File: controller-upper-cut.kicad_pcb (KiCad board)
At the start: 2 copper layers, 32 x 77 mm, 17 parts, among them J1 Conn_01x06_Female, J6 DB25 FEMALE, U2 74HC245, U3 74HC245, U4 ACSL-6310, U5 ACSL-6310

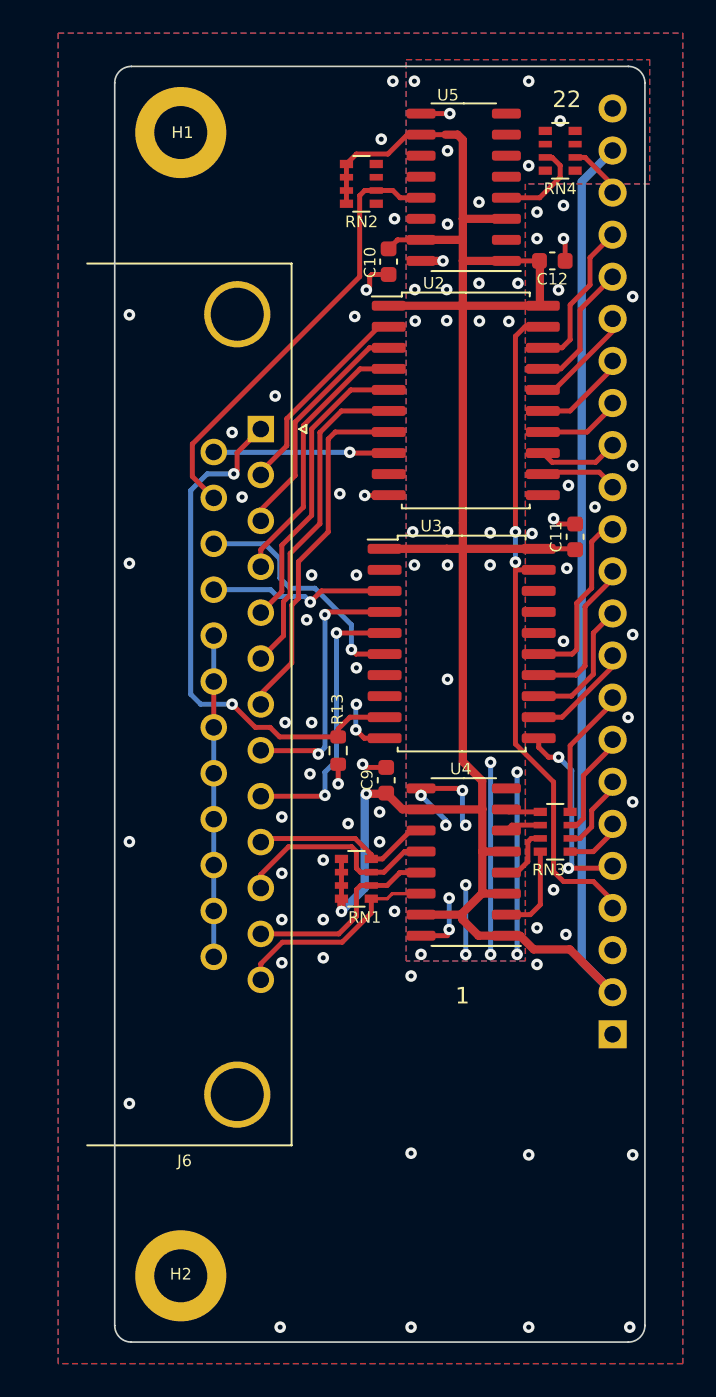
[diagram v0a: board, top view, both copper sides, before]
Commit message: v3.2 pre-production clean-up
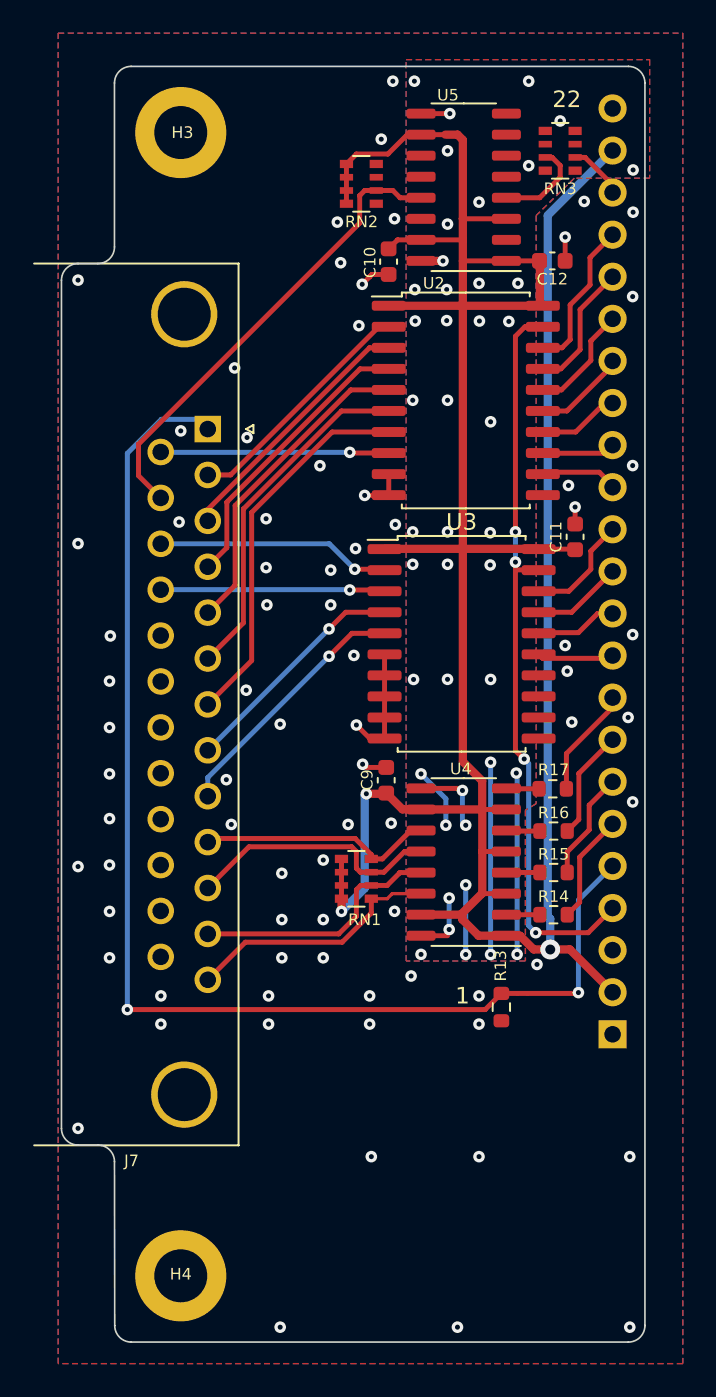
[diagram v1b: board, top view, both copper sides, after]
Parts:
- removed the RN3 at (76.6, 162.2)
- added NT1: NetTie_2, -Project:NetTie-2_SMD_Pad0.3mm, F.Cu at (74.6, 171.9)
- added R14: 330, Resistor_SMD:R_0603_1608Metric, F.Cu at (76.5, 167.2)
- added R15: 330, Resistor_SMD:R_0603_1608Metric, F.Cu at (76.5, 164.7)
- added R16: 330, Resistor_SMD:R_0603_1608Metric, F.Cu at (76.5, 162.2)
- added R17: 330, Resistor_SMD:R_0603_1608Metric, F.Cu at (76.5, 159.6)
- moved R13 18.3 mm to (73.3, 172.8)
- moved J7 3.20 mm to (55.6, 137.9)
- renumbered H1 to H3, H2 to H4, J1 to J2, J6 to J7, RN4 to RN3
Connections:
- J2 pad 3: /HOLD_IN -> unconnected-(J2-Pad3)
- U2 pad 9: unconnected-(U2-Pad9) -> GND1
- U3 pad 11: /LPT Interface/P1_OUT -> unconnected-(U3-Pad11)
- U3 pad 12: /LPT Interface/P9_OUT -> unconnected-(U3-Pad12)
- U3 pad 13: /LPT Interface/P8_OUT -> unconnected-(U3-Pad13)
- U3 pad 14: /LPT Interface/P17_OUT -> unconnected-(U3-Pad14)
- U3 pad 15: /LPT Interface/P16_OUT -> /LPT Interface/P9_OUT
- U3 pad 16: unconnected-(U3-Pad16) -> /LPT Interface/P8_OUT
- U3 pad 17: unconnected-(U3-Pad17) -> /LPT Interface/P17_OUT
- U3 pad 18: unconnected-(U3-Pad18) -> /LPT Interface/P16_OUT
- U3 pad 2: unconnected-(U3-Pad2) -> /LPT Interface/P16_IN
- U3 pad 6: /LPT Interface/P16_IN -> GND1
- U3 pad 7: unconnected-(U3-Pad7) -> GND1
- U3 pad 8: unconnected-(U3-Pad8) -> GND1
- U3 pad 9: /LPT Interface/P1_IN -> GND1
- U4 pad 7: Net-(RN3-Pad1) -> +5VA
- U4 pad 8: unconnected-(U4-Pad8) -> Net-(R17-Pad1)
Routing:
- net /LPT Interface/P1_IN: track 32.2 -> 63.5 mm, vias 2 -> 1
- net GND1: track 31.6 -> 15.3 mm, vias 64 -> 77
- net /LPT Interface/P16_OUT: track 10.9 -> 6.66 mm
- net /LPT Interface/P17_OUT: track 9.50 -> 5.49 mm
- net /LPT Interface/nCE_IN: track 41.3 -> 45.1 mm, vias 2 -> 4
- net Net-(R14-Pad1): track 5.50 -> 2.02 mm
- net /LPT Interface/P13_IN: track 3.33 -> 6.62 mm
- net /LPT Interface/P12_OUT: track 12.1 -> 15.3 mm
- net /LPT Interface/P10_OUT: track 11.1 -> 14.3 mm
- net /LPT Interface/P14_IN: track 10.6 -> 13.8 mm
- net /LPT Interface/P8_OUT: track 8.06 -> 4.96 mm
- net /LPT Interface/P11_OUT: track 12.9 -> 15.6 mm
- net /LPT Interface/P17_IN: track 10.9 -> 13.5 mm
- net /LPT Interface/P13_OUT: track 12.9 -> 15.5 mm
- net /LPT Interface/P2_IN: track 12.5 -> 14.6 mm
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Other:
- board size 32 x 77 mm -> 35.2 x 77 mm
- board text removed: "LPT INTERFACE"

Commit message: more clean-up
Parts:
- added C1: 100n/50V, Capacitor_SMD:C_0603_1608Metric, F.Cu at (74.4, 85.9)
- added C2: 1u/50V, Capacitor_SMD:C_0603_1608Metric, F.Cu at (80.1, 93.2)
- added C3: 1u/50V, Capacitor_SMD:C_0603_1608Metric, F.Cu at (51.4, 77.7)
- added C4: 100u/35V, -Project:CP_Elec_8x10.5_DOT, F.Cu at (63.6, 100.8)
- added C5: 100n/50V, Capacitor_SMD:C_0603_1608Metric, F.Cu at (66.5, 93.1)
- added C6: 100n/50V, Capacitor_SMD:C_0603_1608Metric, F.Cu at (59.5, 89.8)
- added C7: 22u/25V, Capacitor_SMD:C_1206_3216Metric, F.Cu at (71.5, 79.9)
- added C8: 68u/35V, -Project:CP_Elec_6.3x7.7_DOT, F.Cu at (71.0, 92.5)
- added D1: SDM20U40-7, Diode_SMD:D_SOD-523, F.Cu at (75.4, 90.6)
- added D2: SDM20U40-7, Diode_SMD:D_SOD-523, F.Cu at (78.2, 93.3)
- added D3: SDM20U40-7, Diode_SMD:D_SOD-523, F.Cu at (76.4, 93.3)
- added D4: SDM20U40-7, Diode_SMD:D_SOD-523, F.Cu at (77.0, 100.5)
- added D5: SDM20U40-7, Diode_SMD:D_SOD-523, F.Cu at (77.0, 102.2)
- added D6: SS24A+, -Project:D_SMA_DOT, F.Cu at (56.9, 91.6)
- added D7: BAT54JFILM, -Project:D_SOD-323_DOT, F.Cu at (70.9, 45.8)
- added H1: MountingHole_Pad, MountingHole:MountingHole_3.2mm_M3_ISO14580_Pad, F.Cu at (110.0, 120.0)
- added H2: MountingHole_Pad, MountingHole:MountingHole_3.2mm_M3_ISO14580_Pad, F.Cu at (110.0, 189.0)
- added H5: MountingHole_Pad, MountingHole:MountingHole_3.2mm_M3_ISO14580_Pad, F.Cu at (54.0, 34.0)
- added H6: MountingHole_Pad, MountingHole:MountingHole_3.2mm_M3_ISO14580_Pad, F.Cu at (54.0, 103.0)
- added H7: MountingHole_Pad, MountingHole:MountingHole_3.2mm_M3_ISO14580_Pad, F.Cu at (99.5, 34.0)
- added H8: MountingHole_Pad, MountingHole:MountingHole_3.2mm_M3_ISO14580_Pad, F.Cu at (99.5, 103.0)
- added J1: Conn_01x06_Female, Connector_PinSocket_2.54mm:PinSocket_1x23_P2.54mm_Vertical, B.Cu at (136.1, 174.4)
- added J10: Phoenix MPT, TerminalBlock_Phoenix:TerminalBlock_Phoenix_MPT-0,5-6-2.54_1x06_P2.54mm_Horizontal, F.Cu at (109.5, 75.2)
- added J11: Phoenix MPT, TerminalBlock_Phoenix:TerminalBlock_Phoenix_MPT-0,5-4-2.54_1x04_P2.54mm_Horizontal, F.Cu at (109.5, 35.8)
- added J12: MicroFit_2x04, Connector_Molex:Molex_Micro-Fit_3.0_43045-0812_2x04_P3.00mm_Vertical, F.Cu at (86.6, 51.5)
- added J13: Phoenix MPT, TerminalBlock_Phoenix:TerminalBlock_Phoenix_MPT-0,5-4-2.54_1x04_P2.54mm_Horizontal, F.Cu at (109.5, 48.8)
- added J14: MicroFit_2x04, Connector_Molex:Molex_Micro-Fit_3.0_43045-0812_2x04_P3.00mm_Vertical, F.Cu at (86.6, 70.3)
- added J15: JST_B2B-XH, TerminalBlock_Phoenix:TerminalBlock_Phoenix_MPT-0,5-4-2.54_1x04_P2.54mm_Horizontal, F.Cu at (40.7, 84.6)
- added J16: Phoenix MPT, TerminalBlock_Phoenix:TerminalBlock_Phoenix_MPT-0,5-4-2.54_1x04_P2.54mm_Horizontal, F.Cu at (109.5, 62.1)
- added J17: MicroFit_2x04, Connector_Molex:Molex_Micro-Fit_3.0_43045-0812_2x04_P3.00mm_Vertical, F.Cu at (86.6, 89.2)
- added J18: MLX_1x03, Connector_Molex:Molex_KK-254_AE-6410-03A_1x03_P2.54mm_Vertical, F.Cu at (96.7, 78.4)
- added J19: MLX_1x03, Connector_Molex:Molex_KK-254_AE-6410-03A_1x03_P2.54mm_Vertical, F.Cu at (96.7, 88.0)
- added J20: Phoenix MPT, TerminalBlock_Phoenix:TerminalBlock_Phoenix_MPT-0,5-4-2.54_1x04_P2.54mm_Horizontal, F.Cu at (40.7, 53.4)
- added J3: Conn_01x022_Male, Connector_PinHeader_2.54mm:PinHeader_1x23_P2.54mm_Vertical, F.Cu at (80.1, 88.3)
- added J4: KYCON_KPJX-4S-S, -Project:KYCON_KPJX-4S-S, F.Cu at (57.0, 65.5)
- added J5: MicroFit_2x02, Connector_Molex:Molex_Micro-Fit_3.0_43045-0412_2x02_P3.00mm_Vertical, F.Cu at (87.3, 96.9)
- added J6: 24V/5A OUT, TerminalBlock_Phoenix:TerminalBlock_Phoenix_MKDS-1,5-2-5.08_1x02_P5.08mm_Horizontal, F.Cu at (108.0, 99.7)
- added J8: Phoenix MPT, TerminalBlock_Phoenix:TerminalBlock_Phoenix_MPT-0,5-2-2.54_1x02_P2.54mm_Horizontal, F.Cu at (40.7, 77.9)
- added JP1: Jumper_2_Bridged, Connector_PinHeader_2.54mm:PinHeader_2x01_P2.54mm_Vertical, F.Cu at (97.8, 96.5)
- added JP2: GND_ISO, Connector_PinHeader_2.54mm:PinHeader_1x02_P2.54mm_Vertical, F.Cu at (90.7, 33.8)
- added JP3: 1x03_2.54, Connector_PinHeader_2.54mm:PinHeader_1x03_P2.54mm_Vertical, F.Cu at (75.4, 70.1)
- added JP4: Jumper_3_Open, Connector_PinHeader_2.54mm:PinHeader_1x03_P2.54mm_Vertical, F.Cu at (100.2, 45.6)
- added JP5: Jumper_3_Open, Connector_PinHeader_2.54mm:PinHeader_1x03_P2.54mm_Vertical, F.Cu at (100.2, 57.7)
- added JP6: 1x03_2.54, Connector_PinHeader_2.54mm:PinHeader_1x03_P2.54mm_Vertical, F.Cu at (75.4, 63.3)
- added JP7: 1x03_2.54, Connector_PinHeader_2.54mm:PinHeader_1x03_P2.54mm_Vertical, F.Cu at (75.4, 53.5)
- added JP8: Jumper_3_Open, Connector_PinHeader_2.54mm:PinHeader_1x03_P2.54mm_Vertical, F.Cu at (100.2, 68.9)
- added K1: OJS-SH-124HMF, -Project:Relay_SPST_OJS_24V_10A, F.Cu at (67.6, 45.4)
- added L1: 100uH 1.5A+, Inductor_SMD:L_12x12mm_H6mm, F.Cu at (62.5, 81.4)
- added NT22: DNI, -Project:NetTie-2_SMD_Pad0.3mm, F.Cu at (96.1, 98.5)
- added NT23: DNI, -Project:NetTie-2_SMD_Pad1.0mm, F.Cu at (59.5, 97.9)
- added NT24: DNI, -Project:NetTie-2_SMD_Pad1.0mm, F.Cu at (73.1, 82.6)
- added NT25: DNI, -Project:NetTie-2_SMD_Pad0.3mm, B.Cu at (108.3, 81.7)
- added NT26: DNI, -Project:NetTie-2_SMD_Pad0.3mm, B.Cu at (108.3, 79.1)
- added NT27: DNI, -Project:NetTie-2_SMD_Pad0.3mm, B.Cu at (111.5, 74.8)
- added NT28: DNI, -Project:NetTie-2_SMD_Pad1.0mm, B.Cu at (97.6, 64.5)
- added Q1: BC847, Package_TO_SOT_SMD:SOT-23, F.Cu at (77.7, 98.0)
- added Q2: FDD5614P, Package_TO_SOT_SMD:TO-252-2, F.Cu at (49.6, 87.1)
- added Q3: BC857, -Project:SOT-23_DOT, F.Cu at (71.6, 100.8)
- added Q4: BC847, Package_TO_SOT_SMD:SOT-23, F.Cu at (68.5, 64.0)
- added Q5: BC857, -Project:SOT-23_DOT, F.Cu at (66.0, 60.0)
- added R10: 130K, Resistor_SMD:R_0603_1608Metric, F.Cu at (74.8, 101.3)
- added R11: 1M, Resistor_SMD:R_0603_1608Metric, F.Cu at (71.5, 98.0)
- added R12: 220K, Resistor_SMD:R_0603_1608Metric, F.Cu at (66.4, 89.8)
- added R18: 5K6, Resistor_SMD:R_0603_1608Metric, F.Cu at (70.2, 60.4)
- added R19: 5K6, Resistor_SMD:R_0603_1608Metric, F.Cu at (68.5, 60.4)
- added R2: 1M, Resistor_SMD:R_0603_1608Metric, F.Cu at (77.4, 85.9)
- added R20: 10K, Resistor_SMD:R_0603_1608Metric, F.Cu at (66.0, 57.1)
- added R3: 6K8, Resistor_SMD:R_0603_1608Metric, F.Cu at (77.3, 95.4)
- added R4: 220K, Resistor_SMD:R_0603_1608Metric, F.Cu at (51.4, 79.2)
- added R5: 1K, Resistor_SMD:R_0603_1608Metric, F.Cu at (95.1, 98.2)
- added R6: 130K, Resistor_SMD:R_0603_1608Metric, F.Cu at (74.8, 98.0)
- added R7: 1M, Resistor_SMD:R_0603_1608Metric, F.Cu at (51.4, 80.7)
- added R8: 680K, Resistor_SMD:R_0603_1608Metric, F.Cu at (49.0, 79.9)
- added R9: 330K, Resistor_SMD:R_0603_1608Metric, F.Cu at (51.4, 76.2)
- added U1: MAX5035BUSA, Package_SO:SOIC-8_3.9x4.9mm_P1.27mm, F.Cu at (63.0, 92.0)
- added U6: USBLC6-2SC6, Package_TO_SOT_SMD:SOT-23-6, F.Cu at (111.0, 177.5)
- added U7: ADUM4160, Package_SO:SOIC-16W_7.5x10.3mm_P1.27mm, F.Cu at (114.8, 169.3)
- added U8: ATmega16U2-A, Package_QFP:TQFP-32_7x7mm_P0.8mm, F.Cu at (127.1, 169.2)
- added U9: ATmega328P-A, Package_QFP:TQFP-32_7x7mm_P0.8mm, F.Cu at (120.8, 150.9)
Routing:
- net +5V: track 0.00 -> 177.1 mm, vias 0 -> 1
- net 24V_SAFE: track 0.00 -> 119.1 mm, vias 0 -> 52
- net /Connectors & Jumpers/ESTOP_OUT: track 0.00 -> 78.4 mm, vias 0 -> 3
- net /Power/Q1_C: track 0.00 -> 70.0 mm, vias 0 -> 4
- net /Connectors & Jumpers/X_P16_OUT: track 0.00 -> 67.6 mm, vias 0 -> 3
- net /Connectors & Jumpers/EN_IN: track 0.00 -> 65.3 mm
- net /Connectors & Jumpers/X_P17_OUT: track 0.00 -> 53.6 mm, vias 0 -> 3
- net 24V_IN: track 0.00 -> 51.2 mm
- net /Connectors & Jumpers/ZDIR_IN: track 0.00 -> 49.7 mm, vias 0 -> 3
- net /Connectors & Jumpers/VFD_PWM: track 0.00 -> 48.9 mm, vias 0 -> 1
- net /Connectors & Jumpers/ZCLK_IN: track 0.00 -> 48.6 mm, vias 0 -> 2
- net /Connectors & Jumpers/HOLD_OUT: track 0.00 -> 45.5 mm, vias 0 -> 1
- net /Connectors & Jumpers/RELAY4: track 0.00 -> 44.4 mm, vias 0 -> 1
- net /Connectors & Jumpers/RELAY2_IN: track 0.00 -> 44.0 mm, vias 0 -> 3
- net /Connectors & Jumpers/RELAY3_IN: track 0.00 -> 42.1 mm, vias 0 -> 3
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- added copper zone on F.Cu, net /Power/U2_LX
- added copper zone on B.Cu, net 24V_SAFE
- added copper zone on F.Cu, net 24V_SAFE
- added copper zone on B.Cu, net GND
- added copper zone on F.Cu, net GND
- added copper zone on B.Cu, net GNDA
- added copper zone on F.Cu, net GNDA
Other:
- board size 35.2 x 77 mm -> 101.3 x 162.9 mm
- board text added: "* P16"
- board text added: "* P17"
- board text added: "+24V"
- board text added: "+24V IN"
- board text added: "+5V"
- board text added: "0V"
- board text added: "23"
- board text added: "24V"
- board text added: "24V/5A IN"
- board text added: "5A"
- board text added: "5V"
- board text added: "AGND"
- board text added: "BitSetter"
- board text added: "BitZero"
- board text added: "C"
- board text added: "C.P."
- board text added: "CLK"
- board text added: "COM"
- board text added: "COMMON"
- board text added: "CPO"
- board text added: "DGND"
- board text added: "DIR"
- board text added: "G"
- board text added: "JLCJLCJLCJLC"
- board text added: "LED"
- board text added: "LPT INTERFACE"
- board text added: "NC"
- board text added: "NO"
- board text added: "P1"
- board text added: "PWM 5V"
- board text added: "PWM(5V)"
- board text added: "PWR SW"
- board text added: "RELAY"
- board text added: "RELAYS"
- board text added: "RL1/E"
- board text added: "RL2"
- board text added: "RL3"
- board text added: "RL4*"
- board text added: "RLY4 *"
- board text added: "SPDL RLY"
- board text added: "SPINDLE"
- board text added: "SW"
- board text added: "Shapeoko LPT Interface v3.2"
- board text added: "USB GRBL INTERFACE"
- board text added: "X"
- board text added: "X DRV"
- board text added: "X ENDSTOP"
- board text added: "XGND"
- board text added: "Y"
- board text added: "Y DRV"
- board text added: "Y ENDSTOP"
- board text added: "YCLX"
- board text added: "Z"
- board text added: "Z DRV"
- board text added: "Z ENDSTOP"
- board text added: "ZCLX"
- board text added: "github.com/gruvin/shapeoko-lpt"
- board text removed: "22"

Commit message: commit to v3.2 production
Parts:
- removed C1, C5, C6: 100n/50V, Capacitor_SMD:C_0603_1608Metric
- removed C2, C3: 1u/50V, Capacitor_SMD:C_0603_1608Metric
- removed C4: 100u/35V, -Project:CP_Elec_8x10.5_DOT
- removed C7: 22u/25V, Capacitor_SMD:C_1206_3216Metric
- removed C8: 68u/35V, -Project:CP_Elec_6.3x7.7_DOT
- removed D1, D2, D3, D4, D5: SDM20U40-7, Diode_SMD:D_SOD-523
- removed D6: SS24A+, -Project:D_SMA_DOT
- removed D7: BAT54JFILM, -Project:D_SOD-323_DOT
- removed H1, H2, H5, H6, H7, H8: MountingHole_Pad, MountingHole:MountingHole_3.2mm_M3_ISO14580_Pad
- removed J1: Conn_01x06_Female, Connector_PinSocket_2.54mm:PinSocket_1x23_P2.54mm_Vertical
- removed J10: Phoenix MPT, TerminalBlock_Phoenix:TerminalBlock_Phoenix_MPT-0,5-6-2.54_1x06_P2.54mm_Horizontal
- removed J11, J13, J16, J20: Phoenix MPT, TerminalBlock_Phoenix:TerminalBlock_Phoenix_MPT-0,5-4-2.54_1x04_P2.54mm_Horizontal
- removed J12, J14, J17: MicroFit_2x04, Connector_Molex:Molex_Micro-Fit_3.0_43045-0812_2x04_P3.00mm_Vertical
- removed J15: JST_B2B-XH, TerminalBlock_Phoenix:TerminalBlock_Phoenix_MPT-0,5-4-2.54_1x04_P2.54mm_Horizontal
- removed J18, J19: MLX_1x03, Connector_Molex:Molex_KK-254_AE-6410-03A_1x03_P2.54mm_Vertical
- removed J3: Conn_01x022_Male, Connector_PinHeader_2.54mm:PinHeader_1x23_P2.54mm_Vertical
- removed J4: KYCON_KPJX-4S-S, -Project:KYCON_KPJX-4S-S
- removed J5: MicroFit_2x02, Connector_Molex:Molex_Micro-Fit_3.0_43045-0412_2x02_P3.00mm_Vertical
- removed J6: 24V/5A OUT, TerminalBlock_Phoenix:TerminalBlock_Phoenix_MKDS-1,5-2-5.08_1x02_P5.08mm_Horizontal
- removed J8: Phoenix MPT, TerminalBlock_Phoenix:TerminalBlock_Phoenix_MPT-0,5-2-2.54_1x02_P2.54mm_Horizontal
- removed JP1: Jumper_2_Bridged, Connector_PinHeader_2.54mm:PinHeader_2x01_P2.54mm_Vertical
- removed JP2: GND_ISO, Connector_PinHeader_2.54mm:PinHeader_1x02_P2.54mm_Vertical
- removed JP3, JP6, JP7: 1x03_2.54, Connector_PinHeader_2.54mm:PinHeader_1x03_P2.54mm_Vertical
- removed JP4, JP5, JP8: Jumper_3_Open, Connector_PinHeader_2.54mm:PinHeader_1x03_P2.54mm_Vertical
- removed K1: OJS-SH-124HMF, -Project:Relay_SPST_OJS_24V_10A
- removed L1: 100uH 1.5A+, Inductor_SMD:L_12x12mm_H6mm
- removed NT22, NT25, NT26, NT27: DNI, -Project:NetTie-2_SMD_Pad0.3mm
- removed NT23, NT24, NT28: DNI, -Project:NetTie-2_SMD_Pad1.0mm
- removed Q1, Q4: BC847, Package_TO_SOT_SMD:SOT-23
- removed Q2: FDD5614P, Package_TO_SOT_SMD:TO-252-2
- removed Q3, Q5: BC857, -Project:SOT-23_DOT
- removed R10, R6: 130K, Resistor_SMD:R_0603_1608Metric
- removed R11, R2, R7: 1M, Resistor_SMD:R_0603_1608Metric
- removed R12, R4: 220K, Resistor_SMD:R_0603_1608Metric
- removed R18, R19: 5K6, Resistor_SMD:R_0603_1608Metric
- removed R20: 10K, Resistor_SMD:R_0603_1608Metric
- removed R3: 6K8, Resistor_SMD:R_0603_1608Metric
- removed R5: 1K, Resistor_SMD:R_0603_1608Metric
- removed R8: 680K, Resistor_SMD:R_0603_1608Metric
- removed R9: 330K, Resistor_SMD:R_0603_1608Metric
- removed RN3: 1Kx4, Resistor_SMD:R_Array_Convex_4x0603
- removed U1: MAX5035BUSA, Package_SO:SOIC-8_3.9x4.9mm_P1.27mm
- removed U6: USBLC6-2SC6, Package_TO_SOT_SMD:SOT-23-6
- removed U7: ADUM4160, Package_SO:SOIC-16W_7.5x10.3mm_P1.27mm
- removed U8: ATmega16U2-A, Package_QFP:TQFP-32_7x7mm_P0.8mm
- removed U9: ATmega328P-A, Package_QFP:TQFP-32_7x7mm_P0.8mm
- added R22: 330, Resistor_SMD:R_0603_1608Metric, F.Cu at (76.8, 121.5)
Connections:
- RN2 pad 5: unconnected-(RN2-Pad5) -> Net-(U5-Pad14)
- RN2 pad 7: unconnected-(RN2-Pad7) -> Net-(U5-Pad12)
- RN2 pad 8: unconnected-(RN2-Pad8) -> Net-(U5-Pad11)
- U5 pad 11: unconnected-(U5-Pad11) -> Net-(U5-Pad11)
- U5 pad 12: unconnected-(U5-Pad12) -> Net-(U5-Pad12)
- U5 pad 14: unconnected-(U5-Pad14) -> Net-(U5-Pad14)
- U5 pad 5: unconnected-(U5-Pad5) -> +5VA
- U5 pad 7: unconnected-(U5-Pad7) -> +5VA
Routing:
- net +5V: track 177.1 -> 0.00 mm, vias 1 -> 0
- net 24V_SAFE: track 119.1 -> 0.00 mm, vias 52 -> 0
- net /Connectors & Jumpers/ESTOP_OUT: track 78.4 -> 0.00 mm, vias 3 -> 0
- net /Power/Q1_C: track 70.0 -> 0.00 mm, vias 4 -> 0
- net /Connectors & Jumpers/X_P16_OUT: track 67.6 -> 0.00 mm, vias 3 -> 0
- net /Connectors & Jumpers/EN_IN: track 65.3 -> 0.00 mm
- net /Connectors & Jumpers/X_P17_OUT: track 53.6 -> 0.00 mm, vias 3 -> 0
- net 24V_IN: track 51.2 -> 0.00 mm
- net /Connectors & Jumpers/ZDIR_IN: track 49.7 -> 0.00 mm, vias 3 -> 0
- net /Connectors & Jumpers/VFD_PWM: track 48.9 -> 0.00 mm, vias 1 -> 0
- net /Connectors & Jumpers/ZCLK_IN: track 48.6 -> 0.00 mm, vias 2 -> 0
- net /Connectors & Jumpers/HOLD_OUT: track 45.5 -> 0.00 mm, vias 1 -> 0
- net /Connectors & Jumpers/RELAY4: track 44.4 -> 0.00 mm, vias 1 -> 0
- net /Connectors & Jumpers/RELAY2_IN: track 44.0 -> 0.00 mm, vias 3 -> 0
- net /Connectors & Jumpers/RELAY3_IN: track 42.1 -> 0.00 mm, vias 3 -> 0
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- removed copper zone on F.Cu, net /Power/U2_LX
- removed copper zone on B.Cu, net 24V_SAFE
- removed copper zone on F.Cu, net 24V_SAFE
- removed copper zone on B.Cu, net GND
- removed copper zone on F.Cu, net GND
- removed copper zone on B.Cu, net GNDA
- removed copper zone on F.Cu, net GNDA
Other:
- board size 101.3 x 162.9 mm -> 35.2 x 77 mm
- board text removed: "* P16"
- board text removed: "* P17"
- board text removed: "+24V"
- board text removed: "+24V IN"
- board text removed: "+5V"
- board text removed: "0V"
- board text removed: "24V"
- board text removed: "24V/5A IN"
- board text removed: "5A"
- board text removed: "5V"
- board text removed: "AGND"
- board text removed: "BitSetter"
- board text removed: "BitZero"
- board text removed: "C"
- board text removed: "C.P."
- board text removed: "CLK"
- board text removed: "COM"
- board text removed: "COMMON"
- board text removed: "CPO"
- board text removed: "DGND"
- board text removed: "DIR"
- board text removed: "G"
- board text removed: "JLCJLCJLCJLC"
- board text removed: "LED"
- board text removed: "NC"
- board text removed: "NO"
- board text removed: "P1"
- board text removed: "PWM 5V"
- board text removed: "PWM(5V)"
- board text removed: "PWR SW"
- board text removed: "RELAY"
- board text removed: "RELAYS"
- board text removed: "RL1/E"
- board text removed: "RL2"
- board text removed: "RL3"
- board text removed: "RL4*"
- board text removed: "RLY4 *"
- board text removed: "SPDL RLY"
- board text removed: "SPINDLE"
- board text removed: "SW"
- board text removed: "Shapeoko LPT Interface v3.2"
- board text removed: "USB GRBL INTERFACE"
- board text removed: "X"
- board text removed: "X DRV"
- board text removed: "X ENDSTOP"
- board text removed: "XGND"
- board text removed: "Y"
- board text removed: "Y DRV"
- board text removed: "Y ENDSTOP"
- board text removed: "YCLX"
- board text removed: "Z"
- board text removed: "Z DRV"
- board text removed: "Z ENDSTOP"
- board text removed: "ZCLX"
- board text removed: "github.com/gruvin/shapeoko-lpt"
